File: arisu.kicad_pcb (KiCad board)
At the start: 2 copper layers, 373.1 x 110.3 mm, 136 parts, among them J1 USB_B_Micro, J10 PF6, J11 PF7, J12 VCC, J13 D+, J14 D-, J15 GND, J2 MISO, J3 VCC, J4 SCK, J5 MOSI, J6 RES, J7 GND, J8 PF4, J9 PF5, SW11 SW_Push, SW12 SW_Push, SW13 SW_Push, SW14 SW_Push, SW16 SW_Push, SW17 SW_Push, SW18 SW_Push, SW2 SW_Push, SW20 SW_Push, SW21 SW_Push, SW22 SW_Push, SW23 SW_Push, SW25 SW_Push, SW26 SW_Push, SW27 SW_Push, SW28 SW_Push, SW3 SW_Push, SW30 SW_Push, SW31 SW_Push, SW32 SW_Push, SW34 SW_Push, SW35 SW_Push, SW36 SW_Push, SW37 SW_Push, SW39 SW_Push, SW4 SW_Push, SW40 SW_Push, SW41 SW_Push, SW43 SW_Push, SW44 SW_Push, SW45 SW_Push, SW46 SW_Push, SW48 SW_Push, SW49 SW_Push, SW5 SW_Push, SW50 SW_Push, SW52 SW_Push, SW53 SW_Push, SW54 SW_Push, SW56 SW_Push, SW57 SW_Push, SW58 SW_Push, SW62 SW_Push, SW63 SW_Push, SW64 SW_Push, SW7 SW_Push, SW8 SW_Push, SW9 SW_Push, U1 USBLC6-2SC6, U2 ATmega32U4-AU, Y1 Crystal_GND24

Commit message: Route yet more tracks.
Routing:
- net VCC: track 67.3 -> 205.8 mm, vias 3 -> 9
- net /col0: track 80.1 -> 211.6 mm, vias 0 -> 3
- net /col1: track 53.3 -> 157.7 mm, vias 0 -> 1
- net /col9: track 81.7 -> 173.3 mm, vias 0 -> 1
- net /col2: track 89.6 -> 164.9 mm, vias 0 -> 3
- net /col3: track 52.1 -> 114.0 mm, vias 0 -> 1
- net GND: track 41.4 -> 74.5 mm, vias 8 -> 12
- net /col4: track 81.0 -> 113.7 mm, vias 0 -> 1
- net Net-(J1-Pad3): track 15.6 -> 47.9 mm
- net /~RES~: track 3.94 -> 35.1 mm, vias 0 -> 2
- net /col6: track 47.2 -> 74.4 mm, vias 0 -> 1
- net /col5: track 82.3 -> 99.9 mm, vias 0 -> 1
- net Net-(J1-Pad2): track 32.9 -> 44.5 mm

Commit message: Connect a couple stray pads and complete DRC.
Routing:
- net /col12: track 86.2 -> 283.8 mm, vias 0 -> 3
- net /col11: track 50.9 -> 223.6 mm, vias 0 -> 3
- net /col10: track 84.0 -> 242.4 mm, vias 0 -> 3
- net /row3: track 370.3 -> 457.5 mm, vias 0 -> 2
- net /col8: track 86.1 -> 165.5 mm, vias 0 -> 1
- net /SCK: track 105.4 -> 177.7 mm, vias 0 -> 3
- net /row2: track 420.6 -> 481.7 mm, vias 0 -> 2
- net /row1: track 373.1 -> 426.5 mm, vias 0 -> 2
- net /MISO: track 0.00 -> 50.1 mm, vias 0 -> 1
- net /PF7: track 0.00 -> 45.5 mm, vias 0 -> 1
- net /MOSI: track 0.00 -> 44.0 mm, vias 0 -> 1
- net /PF6: track 0.00 -> 43.1 mm, vias 0 -> 1
- net /PF5: track 0.00 -> 40.7 mm, vias 0 -> 1
- net /row0: track 349.7 -> 388.8 mm, vias 0 -> 2
- net /PF4: track 0.00 -> 38.3 mm, vias 0 -> 1
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
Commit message: Start to rework for tighter layout and better ergonomicityness.
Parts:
- moved SW25 180.4 mm to (88.5, -92.4), turned to 348 degrees
- moved D25 179.8 mm to (91.9, -78.1), turned to 78 degrees
- moved SW20 179.5 mm to (69.9, -96.3), turned to 348 degrees
- moved D20 178.6 mm to (73.3, -82.0), turned to 78 degrees
- moved SW28 175.9 mm to (62.7, -39.4)
- moved D23 175.9 mm to (47.7, -29.1)
- moved D28 175.9 mm to (77.0, -22.7)
- moved SW23 175.9 mm to (44.1, -43.4)
- moved SW26 175.8 mm to (79.9, -74.7), turned to 348 degrees
- moved D26 175.8 mm to (83.3, -60.4), turned to 78 degrees
- moved SW21 174.9 mm to (61.3, -78.7), turned to 348 degrees
- moved D21 174.3 mm to (64.7, -64.4), turned to 78 degrees
- moved SW27 171.3 mm to (71.3, -57.1), turned to 348 degrees
- moved D27 170.7 mm to (74.7, -42.8), turned to 78 degrees
- moved SW22 170.4 mm to (52.6, -61.1), turned to 348 degrees
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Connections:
- C1 pad 1: GND -> (no net)
- C1 pad 2: XTAL1 -> (no net)
- C2 pad 1: XTAL2 -> (no net)
- C2 pad 2: GND -> (no net)
- C3 pad 1: VCC -> (no net)
- C3 pad 2: GND -> (no net)
- C4 pad 1: Net-(C4-Pad1) -> (no net)
- C4 pad 2: GND -> (no net)
- C5 pad 1: VCC -> (no net)
- C5 pad 2: GND -> (no net)
- C6 pad 1: VCC -> (no net)
- C6 pad 2: GND -> (no net)
- C7 pad 1: VCC -> (no net)
- C7 pad 2: GND -> (no net)
- C8 pad 1: VCC -> (no net)
- C8 pad 2: GND -> (no net)
- C9 pad 1: VCC -> (no net)
- C9 pad 2: GND -> (no net)
- J1 pad 1: VCC -> (no net)
- J1 pad 2: Net-(J1-Pad2) -> (no net)
- J1 pad 3: Net-(J1-Pad3) -> (no net)
- J1 pad 5: GND -> (no net)
- J1 pad 6: GND -> (no net)
- R1 pad 1: D+ -> (no net)
- R1 pad 2: Net-(J1-Pad3) -> (no net)
- R2 pad 1: D- -> (no net)
- R2 pad 2: Net-(J1-Pad2) -> (no net)
- R3 pad 1: VCC -> (no net)
- R3 pad 2: /~RES~ -> (no net)
- R4 pad 1: Net-(R4-Pad1) -> (no net)
- R4 pad 2: GND -> (no net)
- SWR1 pad 1: GND -> (no net)
- SWR1 pad 2: /~RES~ -> (no net)
- U1 pad 2: GND -> (no net)
- U1 pad 4: Net-(J1-Pad2) -> (no net)
- U1 pad 5: VCC -> (no net)
- U1 pad 6: Net-(J1-Pad3) -> (no net)
- U2 pad 1: /col2 -> (no net)
- U2 pad 10: /MOSI -> (no net)
- U2 pad 11: /MISO -> (no net)
- U2 pad 12: /col9 -> (no net)
- U2 pad 13: /~RES~ -> (no net)
- U2 pad 14: VCC -> (no net)
- U2 pad 15: GND -> (no net)
- U2 pad 16: XTAL2 -> (no net)
- U2 pad 17: XTAL1 -> (no net)
- U2 pad 18: /row0 -> (no net)
- U2 pad 19: /row1 -> (no net)
- U2 pad 2: VCC -> (no net)
- U2 pad 20: /row2 -> (no net)
- U2 pad 21: /row3 -> (no net)
- U2 pad 23: GND -> (no net)
- U2 pad 24: VCC -> (no net)
- U2 pad 25: /col6 -> (no net)
- U2 pad 27: /col12 -> (no net)
- U2 pad 28: /col11 -> (no net)
- U2 pad 29: /col10 -> (no net)
- U2 pad 3: D- -> (no net)
- U2 pad 30: /col5 -> (no net)
- U2 pad 31: /col4 -> (no net)
- U2 pad 32: /col3 -> (no net)
- U2 pad 33: Net-(R4-Pad1) -> (no net)
- U2 pad 34: VCC -> (no net)
- U2 pad 35: GND -> (no net)
- U2 pad 36: /PF7 -> (no net)
- U2 pad 37: /PF6 -> (no net)
- U2 pad 38: /PF5 -> (no net)
- U2 pad 39: /PF4 -> (no net)
- U2 pad 4: D+ -> (no net)
- U2 pad 40: /col1 -> (no net)
- U2 pad 41: /col0 -> (no net)
- U2 pad 43: GND -> (no net)
- U2 pad 44: VCC -> (no net)
- U2 pad 5: GND -> (no net)
- U2 pad 6: Net-(C4-Pad1) -> (no net)
- U2 pad 7: VCC -> (no net)
- U2 pad 8: /col8 -> (no net)
- U2 pad 9: /SCK -> (no net)
- Y1 pad 1: XTAL1 -> (no net)
- Y1 pad 2: GND -> (no net)
- Y1 pad 3: XTAL2 -> (no net)
- Y1 pad 4: GND -> (no net)
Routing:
- net (no net): track 0.00 -> 610.5 mm, vias 0 -> 31
- net /row2: track 481.7 -> 0.00 mm, vias 2 -> 0
- net /row3: track 457.5 -> 0.00 mm, vias 2 -> 0
- net /row1: track 426.5 -> 0.00 mm, vias 2 -> 0
- net /row0: track 388.8 -> 0.00 mm, vias 2 -> 0
- net /col12: track 283.8 -> 0.00 mm, vias 3 -> 0
- net /col10: track 242.4 -> 0.00 mm, vias 3 -> 0
- net /col11: track 223.6 -> 0.00 mm, vias 3 -> 0
- net VCC: track 213.1 -> 0.00 mm, vias 9 -> 0
- net /col0: track 211.6 -> 0.00 mm, vias 3 -> 0
- net /SCK: track 177.7 -> 0.00 mm, vias 3 -> 0
- net /col9: track 173.5 -> 0.00 mm, vias 3 -> 0
- net /col8: track 165.5 -> 0.00 mm, vias 1 -> 0
- net /col2: track 164.9 -> 0.00 mm, vias 3 -> 0
- net /col1: track 157.7 -> 0.00 mm, vias 1 -> 0
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- added copper zone on B.Cu, net (none)

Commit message: Make ergo layout.
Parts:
- SW28: footprint MX_Switch:SW_Cherry_MX_2.25u_PCB_ReversedStabilizers -> MX_Switch:SW_Cherry_MX_2.00u_PCB_ReversedStabilizers
- SW37: footprint MX_Switch:SW_Cherry_MX_2.25u_PCB_ReversedStabilizers -> MX_Switch:SW_Cherry_MX_2.75u_PCB_ReversedStabilizers
- SW46: footprint MX_Switch:SW_Cherry_MX_1.50u_PCB -> MX_Switch:SW_Cherry_MX_1.00u_PCB
- SW54: footprint MX_Switch:SW_Cherry_MX_2.75u_PCB -> MX_Switch:SW_Cherry_MX_1.75u_PCB
- moved SW41 184.7 mm to (163.7, -59.1)
- moved D41 184.7 mm to (172.1, -47.2)
- moved D58 184.0 mm to (247.8, -24.1)
- moved SW58 184.0 mm to (237.1, -37.4)
- moved SW40 182.7 mm to (159.7, -77.7)
- moved D40 182.6 mm to (168.1, -65.8)
- moved D54 181.6 mm to (240.0, -43.2)
- moved SW39 180.7 mm to (155.7, -96.3)
- moved D39 180.7 mm to (164.1, -84.4)
- moved SW45 180.4 mm to (183.3, -58.4)
- moved D45 180.4 mm to (191.7, -46.5)
- moved SW44 178.3 mm to (179.3, -77.0)
- moved D44 178.3 mm to (187.7, -65.1)
- moved D64 176.9 mm to (262.9, -81.5)
- moved D52 176.6 mm to (224.8, -81.5)
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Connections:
- C1 pad 1: (no net) -> GND
- C1 pad 2: (no net) -> XTAL1
- C2 pad 1: (no net) -> XTAL2
- C2 pad 2: (no net) -> GND
- C3 pad 1: (no net) -> VCC
- C3 pad 2: (no net) -> GND
- C4 pad 1: (no net) -> Net-(C4-Pad1)
- C4 pad 2: (no net) -> GND
- C5 pad 1: (no net) -> VCC
- C5 pad 2: (no net) -> GND
- C6 pad 1: (no net) -> VCC
- C6 pad 2: (no net) -> GND
- C7 pad 1: (no net) -> VCC
- C7 pad 2: (no net) -> GND
- C8 pad 1: (no net) -> VCC
- C8 pad 2: (no net) -> GND
- C9 pad 1: (no net) -> VCC
- C9 pad 2: (no net) -> GND
- D63 pad 1: /row3 -> /row2
- D64 pad 1: /row2 -> /row3
- J1 pad 1: (no net) -> VCC
- J1 pad 2: (no net) -> Net-(J1-Pad2)
- J1 pad 3: (no net) -> Net-(J1-Pad3)
- J1 pad 4: (no net) -> Net-(J1-Pad4)
- J1 pad 5: (no net) -> GND
- J1 pad 6: (no net) -> GND
- R1 pad 1: (no net) -> D+
- R1 pad 2: (no net) -> Net-(J1-Pad3)
- R2 pad 1: (no net) -> D-
- R2 pad 2: (no net) -> Net-(J1-Pad2)
- R3 pad 1: (no net) -> VCC
- R3 pad 2: (no net) -> /~RES~
- R4 pad 1: (no net) -> Net-(R4-Pad1)
- R4 pad 2: (no net) -> GND
- SW63 pad 1: /col10 -> /col12
- SWR1 pad 1: (no net) -> GND
- SWR1 pad 2: (no net) -> /~RES~
- U1 pad 1: (no net) -> Net-(U1-Pad1)
- U1 pad 2: (no net) -> GND
- U1 pad 3: (no net) -> Net-(U1-Pad3)
- U1 pad 4: (no net) -> Net-(J1-Pad2)
- U1 pad 5: (no net) -> VCC
- U1 pad 6: (no net) -> Net-(J1-Pad3)
- U2 pad 1: (no net) -> /col2
- U2 pad 10: (no net) -> /MOSI
- U2 pad 11: (no net) -> /MISO
- U2 pad 12: (no net) -> /col9
- U2 pad 13: (no net) -> /~RES~
- U2 pad 14: (no net) -> VCC
- U2 pad 15: (no net) -> GND
- U2 pad 16: (no net) -> XTAL2
- U2 pad 17: (no net) -> XTAL1
- U2 pad 18: (no net) -> /row0
- U2 pad 19: (no net) -> /row1
- U2 pad 2: (no net) -> VCC
- U2 pad 20: (no net) -> /row2
- U2 pad 21: (no net) -> /row3
- U2 pad 22: (no net) -> Net-(U2-Pad22)
- U2 pad 23: (no net) -> GND
- U2 pad 24: (no net) -> VCC
- U2 pad 25: (no net) -> /col6
- U2 pad 26: (no net) -> Net-(U2-Pad26)
- U2 pad 27: (no net) -> /col12
- U2 pad 28: (no net) -> /col11
- U2 pad 29: (no net) -> /col10
- U2 pad 3: (no net) -> D-
- U2 pad 30: (no net) -> /col5
- U2 pad 31: (no net) -> /col4
- U2 pad 32: (no net) -> /col3
- U2 pad 33: (no net) -> Net-(R4-Pad1)
- U2 pad 34: (no net) -> VCC
- U2 pad 35: (no net) -> GND
- U2 pad 36: (no net) -> /PF7
- U2 pad 37: (no net) -> /PF6
- U2 pad 38: (no net) -> /PF5
- U2 pad 39: (no net) -> /PF4
- U2 pad 4: (no net) -> D+
- U2 pad 40: (no net) -> /col1
- U2 pad 41: (no net) -> /col0
- U2 pad 42: (no net) -> Net-(U2-Pad42)
- U2 pad 43: (no net) -> GND
- U2 pad 44: (no net) -> VCC
- U2 pad 5: (no net) -> GND
- U2 pad 6: (no net) -> Net-(C4-Pad1)
- U2 pad 7: (no net) -> VCC
- U2 pad 8: (no net) -> /col8
- U2 pad 9: (no net) -> /SCK
- Y1 pad 1: (no net) -> XTAL1
- Y1 pad 2: (no net) -> GND
- Y1 pad 3: (no net) -> XTAL2
- Y1 pad 4: (no net) -> GND
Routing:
- net (no net): track 610.5 -> 0.00 mm, vias 31 -> 0
- net VCC: track 0.00 -> 136.5 mm, vias 0 -> 6
- net GND: track 0.00 -> 74.2 mm, vias 0 -> 12
- net /MISO: track 0.00 -> 42.8 mm, vias 0 -> 1
- net /MOSI: track 0.00 -> 37.2 mm, vias 0 -> 1
- net Net-(J1-Pad2): track 0.00 -> 33.6 mm
- net /~RES~: track 0.00 -> 32.7 mm, vias 0 -> 2
- net /SCK: track 0.00 -> 31.8 mm
- net /col5: track 0.00 -> 26.6 mm, vias 0 -> 1
- net Net-(J1-Pad3): track 0.00 -> 23.5 mm
- net D-: track 0.00 -> 23.2 mm
- net D+: track 0.00 -> 22.5 mm
- net /row0: track 0.00 -> 15.3 mm, vias 0 -> 1
- net XTAL1: track 0.00 -> 13.1 mm
- net XTAL2: track 0.00 -> 12.7 mm
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- removed copper zone on B.Cu, net (none)

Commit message: Finish ergo layout and route some rows.
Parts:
- removed J10: PF6, Pin_Headers:Pin_Header_Straight_1x01_Pitch2.54mm
- removed J11: PF7, Pin_Headers:Pin_Header_Straight_1x01_Pitch2.54mm
- removed J12, J3: VCC, Pin_Headers:Pin_Header_Straight_1x01_Pitch2.54mm
- removed J13: D+, Pin_Headers:Pin_Header_Straight_1x01_Pitch2.54mm
- removed J14: D-, Pin_Headers:Pin_Header_Straight_1x01_Pitch2.54mm
- removed J15, J7: GND, Pin_Headers:Pin_Header_Straight_1x01_Pitch2.54mm
- removed J2: MISO, Pin_Headers:Pin_Header_Straight_1x01_Pitch2.54mm
- removed J4: SCK, Pin_Headers:Pin_Header_Straight_1x01_Pitch2.54mm
- removed J5: MOSI, Pin_Headers:Pin_Header_Straight_1x01_Pitch2.54mm
- removed J6: RES, Pin_Headers:Pin_Header_Straight_1x01_Pitch2.54mm
- removed J8: PF4, Pin_Headers:Pin_Header_Straight_1x01_Pitch2.54mm
- removed J9: PF5, Pin_Headers:Pin_Header_Straight_1x01_Pitch2.54mm
- moved D11 172.7 mm to (120.9, 64.6)
- moved D12 172.7 mm to (116.9, 83.2)
- moved D16 172.7 mm to (140.5, 63.9)
- moved D18 172.7 mm to (132.6, 101.1)
- moved D2 172.7 mm to (75.3, 68.6)
- moved D20 172.7 mm to (157.2, 77.2)
- moved D23 172.7 mm to (143.3, 142.2)
- moved D26 172.7 mm to (170.8, 104.4)
- moved D3 172.7 mm to (68.9, 87.7)
- moved D30 172.7 mm to (215.7, 87.3)
- moved D34 172.7 mm to (233.3, 78.7)
- moved D37 172.7 mm to (225.8, 143.3)
- moved D39 172.7 mm to (250.0, 65.4)
- moved D40 172.7 mm to (253.9, 84.1)
- moved D44 172.7 mm to (273.6, 84.8)
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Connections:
- net /SCK renamed /col7
- net /~RES~ renamed Net-(R3-Pad2)
- U2 pad 10: /MOSI -> Net-(U2-Pad10)
- U2 pad 11: /MISO -> Net-(U2-Pad11)
- U2 pad 36: /PF7 -> Net-(U2-Pad36)
- U2 pad 37: /PF6 -> Net-(U2-Pad37)
- U2 pad 38: /PF5 -> Net-(U2-Pad38)
- U2 pad 39: /PF4 -> Net-(U2-Pad39)
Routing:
- net /row0: track 15.3 -> 322.8 mm
- net /row1: track 12.5 -> 309.9 mm
- net /row2: track 6.54 -> 303.0 mm
- net /col0: track 1.10 -> 62.8 mm
- net D-: track 23.2 -> 2.56 mm
- net D+: track 22.5 -> 2.52 mm
- net /col5: track 26.6 -> 12.9 mm
- net VCC: track 136.5 -> 124.3 mm
- net /col7: track 31.8 -> 21.8 mm
- net Net-(C4-Pad1): track 12.3 -> 3.98 mm
- net /MOSI: track 37.2 -> 32.3 mm, vias 1 -> 0
- net Net-(U2-Pad10): track 0.00 -> 4.99 mm, vias 0 -> 1
- net Net-(D14-Pad2): track 0.00 -> 4.92 mm
- net Net-(D4-Pad2): track 0.00 -> 4.91 mm
- net Net-(D2-Pad2): track 0.00 -> 4.91 mm
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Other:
- board size 373.1 x 110.3 mm -> 373.1 x 140.4 mm

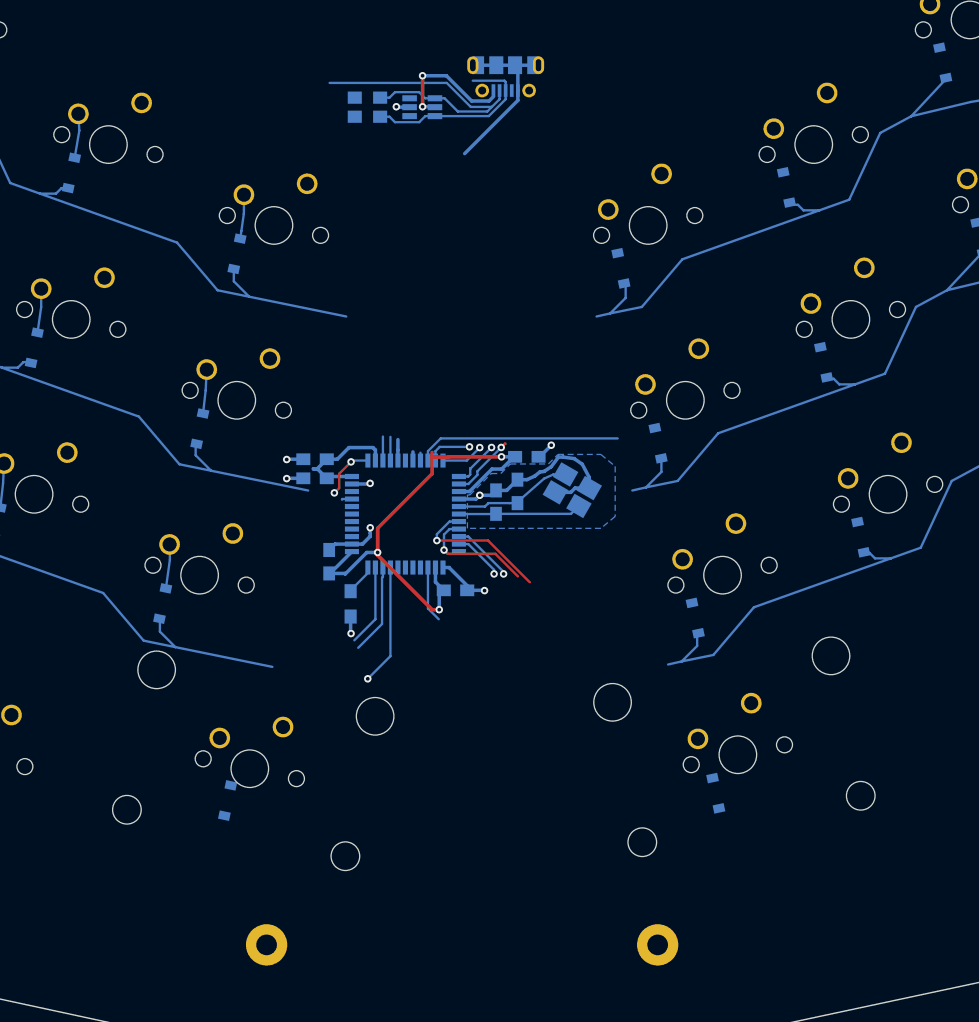
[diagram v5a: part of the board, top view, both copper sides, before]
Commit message: Swap out micro-USB for USB-C 2.0
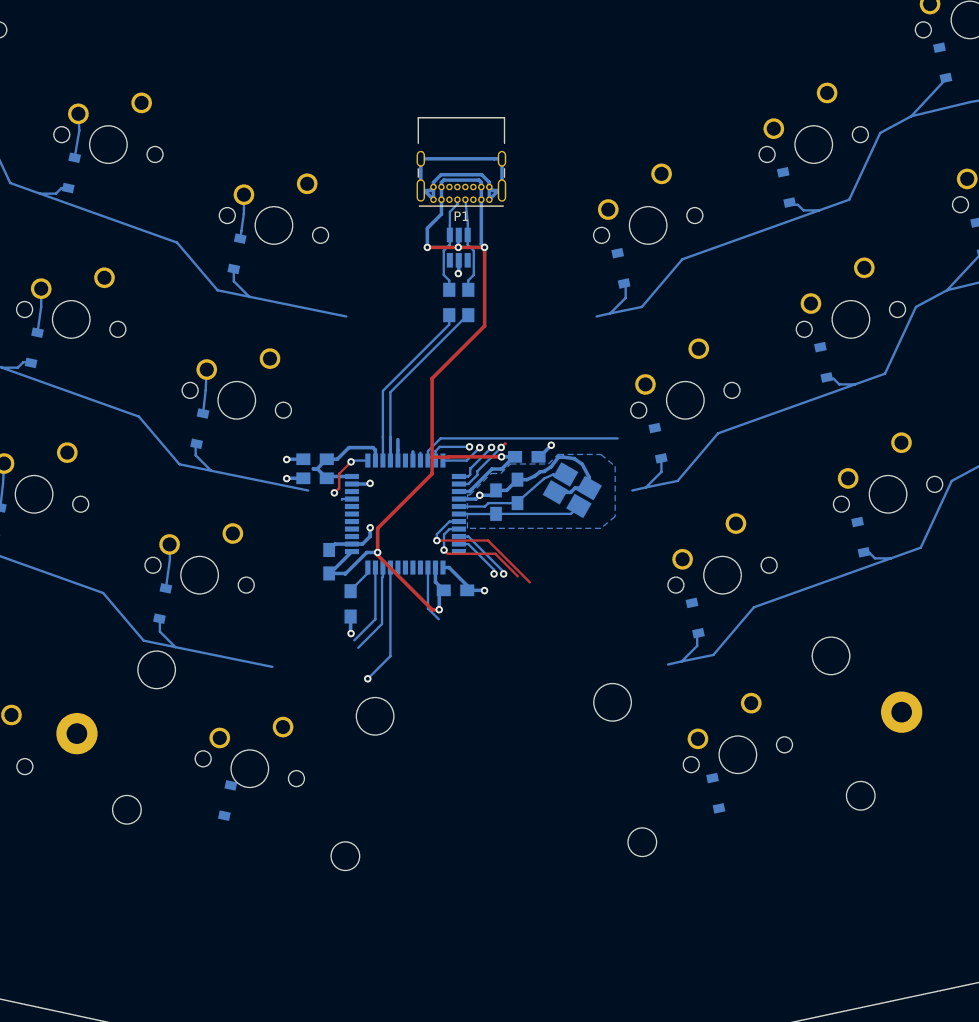
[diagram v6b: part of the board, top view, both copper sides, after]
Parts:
- removed J1: USB_B_Micro, Connectors_USB:USB_Micro-B_Molex-105017-0001
- added P1: USB_C_Plug_USB2.0, Connector_USB:USB_C_Receptacle_GCT_USB4085, F.Cu at (201.7, 80.0)
- moved H6 35.9 mm to (245.6, 134.6)
- moved H4 30.3 mm to (157.7, 136.9)
- moved R2 23.5 mm to (197.4, 91.0), turned to 90 degrees
- moved R1 22.5 mm to (199.4, 91.0), turned to 90 degrees
- moved U1 15.5 mm to (198.4, 85.1), turned to 90 degrees
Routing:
- net VCC: track 124.3 -> 161.5 mm, vias 6 -> 7
- net Net-(P1-PadA7): track 33.6 -> 10.4 mm
- net D+: track 2.52 -> 21.5 mm
- net D-: track 2.56 -> 18.5 mm
- net GND: track 73.7 -> 88.7 mm
- net Net-(P1-PadA6): track 20.0 -> 10.1 mm

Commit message: Route more traces.
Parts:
- moved R3 55.3 mm to (202.9, 103.6), turned to 90 degrees
- moved SWR1 53.0 mm to (210.5, 101.4)
- moved C3 42.4 mm to (207.3, 91.0)
- moved C4 42.0 mm to (203.2, 91.0)
- moved D46 4.93 mm to (261.6, 140.7)
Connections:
- SW64 pad 1: /col12 -> /col11
- U2 pad 18: /row0 -> /col8
- U2 pad 19: /row1 -> /col7
- U2 pad 8: /col8 -> /row0
- U2 pad 9: /col7 -> /row1
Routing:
- net /col12: track 0.00 -> 84.8 mm
- net /col2: track 5.89 -> 81.6 mm, vias 2 -> 0
- net /col4: track 9.65 -> 81.9 mm
- net /row1: track 309.9 -> 377.0 mm, vias 1 -> 3
- net /col5: track 12.9 -> 69.5 mm, vias 1 -> 0
- net /col1: track 0.00 -> 44.1 mm
- net /MISO: track 38.3 -> 0.00 mm
- net /col3: track 8.69 -> 44.5 mm
- net /MOSI: track 32.3 -> 0.00 mm
- net /row0: track 322.8 -> 352.8 mm, vias 1 -> 2
- net VCC: track 161.5 -> 141.6 mm, vias 7 -> 8
- net Net-(C4-Pad1): track 3.98 -> 19.9 mm
- net /col8: track 0.84 -> 15.3 mm, vias 0 -> 1
- net Net-(R3-Pad2): track 32.7 -> 22.9 mm, vias 2 -> 0
- net /col0: track 62.8 -> 72.5 mm
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
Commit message: Route a bunch of columns.
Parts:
- moved D28 1.66 mm to (172.2, 143.5)
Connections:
- U2 pad 1: /col2 -> Net-(U2-Pad1)
- U2 pad 10: Net-(U2-Pad10) -> /col8
- U2 pad 11: Net-(U2-Pad11) -> /col7
- U2 pad 12: /col9 -> /col6
- U2 pad 18: /col8 -> Net-(U2-Pad18)
- U2 pad 19: /col7 -> Net-(U2-Pad19)
- U2 pad 25: /col6 -> /col9
- U2 pad 30: /col5 -> Net-(U2-Pad30)
- U2 pad 31: /col4 -> Net-(U2-Pad31)
- U2 pad 32: /col3 -> Net-(U2-Pad32)
- U2 pad 36: Net-(U2-Pad36) -> /col5
- U2 pad 37: Net-(U2-Pad37) -> /col4
- U2 pad 38: Net-(U2-Pad38) -> /col3
- U2 pad 39: Net-(U2-Pad39) -> /col2
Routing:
- net /row3: track 5.32 -> 391.6 mm
- net /col8: track 15.3 -> 161.3 mm
- net /col7: track 12.5 -> 148.8 mm, vias 1 -> 3
- net /col0: track 72.5 -> 197.4 mm, vias 0 -> 1
- net /col1: track 44.1 -> 140.7 mm, vias 0 -> 1
- net /col9: track 0.00 -> 95.8 mm
- net /col11: track 0.00 -> 83.3 mm
- net /col2: track 81.6 -> 151.7 mm, vias 0 -> 1
- net /col6: track 5.98 -> 74.9 mm, vias 0 -> 1
- net /col3: track 44.5 -> 104.0 mm, vias 0 -> 3
- net /col10: track 0.00 -> 46.4 mm
- net /col4: track 81.9 -> 111.9 mm, vias 0 -> 1
- net /row2: track 303.0 -> 331.0 mm
- net /row1: track 377.0 -> 399.1 mm
- net Net-(U2-Pad18): track 0.00 -> 15.3 mm, vias 0 -> 1
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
